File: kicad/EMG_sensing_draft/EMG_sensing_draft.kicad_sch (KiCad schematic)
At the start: 99 parts, among them J1 USB_A_0480370001, J2 EMG_SIGNAL, J3 DEBUG, U1 MCP6N11-002E/SN, U2 W25Q128JV, U3 ISL90462WIH627Z-TKCT-ND, U4 RP2040, U5 RN4871-I/RM140, U6 MCP1702T-3302E_CB, U8 MCP6024T-E/ST, Y1 12MHz

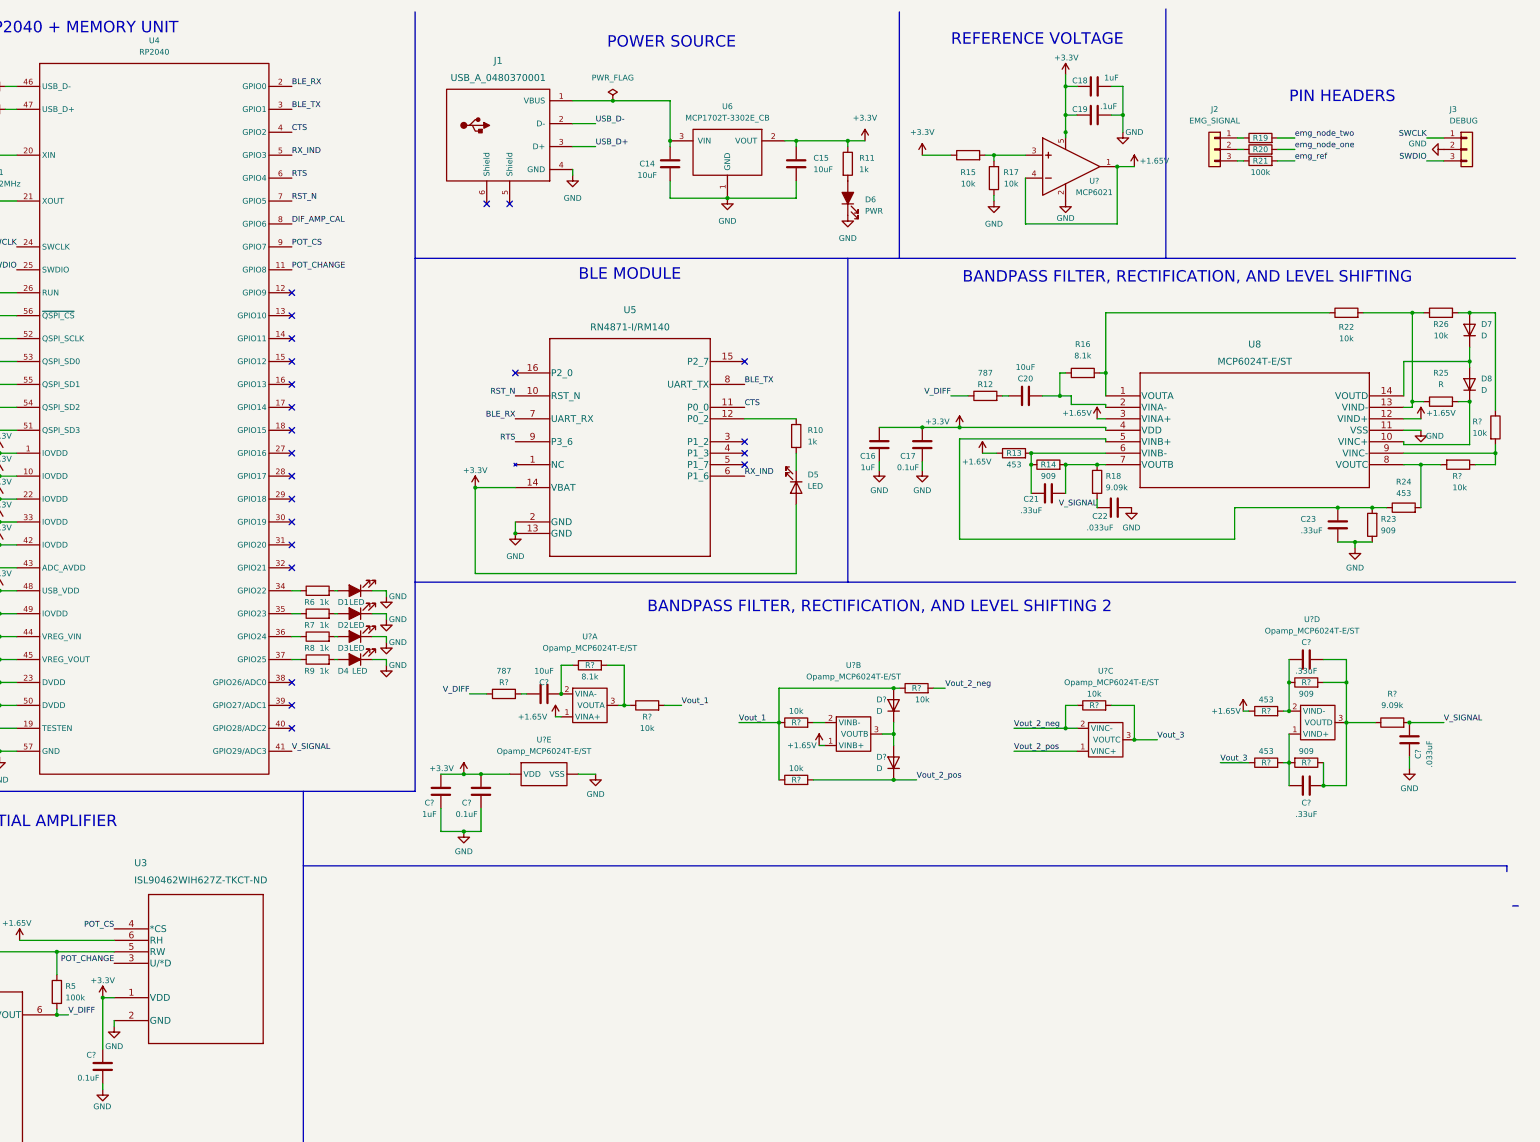
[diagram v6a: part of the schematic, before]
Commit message: fixed ble pin connection
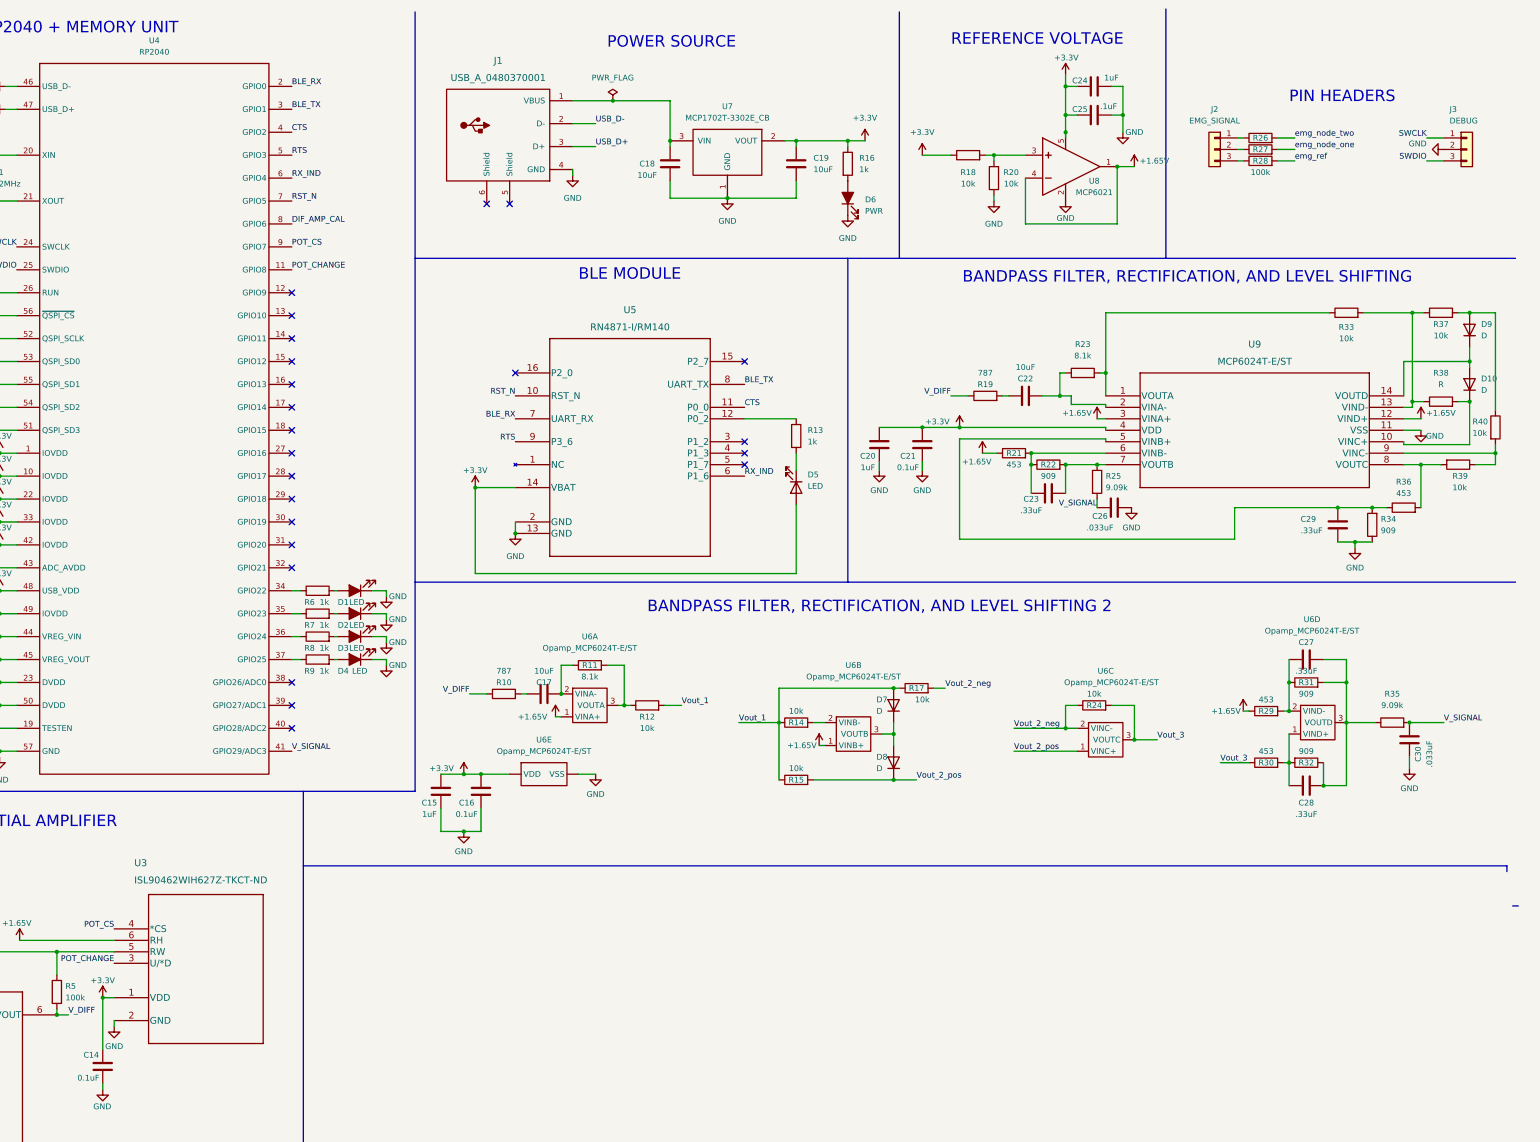
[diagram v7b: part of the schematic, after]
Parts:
- gave numbers to parts that had none: 25
- renumbered C14 to C18, C15 to C19, C16 to C20, C17 to C21, C20 to C22, C21 to C23, C18 to C24, C19 to C25, C22 to C26, C23 to C29, D8 to D10, D7 to D9, R10 to R13, R11 to R16, R15 to R18, R12 to R19, R17 to R20, R13 to R21, R14 to R22, R16 to R23, R18 to R25, R19 to R26, R20 to R27, R21 to R28, R22 to R33, R23 to R34, R24 to R36, R26 to R37, R25 to R38, U6 to U7, U8 to U9
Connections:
- net RTS: now also U4.5 (GPIO3); no longer U4.6 (GPIO4)
- net RX_IND: now also U4.6 (GPIO4); no longer U4.5 (GPIO3)

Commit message: Add Brad suggestions
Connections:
- net +1.65V: now also U3.5 (RW); no longer U3.6 (RH)
- net RTS: now also U4.6 (GPIO4); no longer U4.5 (GPIO3)
- net RX_IND: now also U4.5 (GPIO3); no longer U4.6 (GPIO4)
- net at R5.2, U1.1 (VFG): now also U3.6 (RH); no longer U3.5 (RW)
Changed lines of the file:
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@@
   (junction (at 22.86 105.41) (diameter 0) (color 0 0 0 0)
   )
-  (junction (at 85.09 220.98) (diameter 0) (color 0 0 0 0)
-  )
   (junction (at 398.145 90.17) (diameter 0) (color 0 0 0 0)
   )
+  (junction (at 85.09 220.98) (diameter 0) (color 0 0 0 0)
+  )
   (junction (at 403.86 110.49) (diameter 0) (color 0 0 0 0)
   )
@@
     (stroke (width 0) (type default) (color 0 0 0 0))
   )
-  (wire (pts (xy 85.09 220.98) (xy 97.79 220.98))
-    (stroke (width 0) (type default) (color 0 0 0 0))
-  )
   (wire (pts (xy 290.83 44.45) (xy 292.735 44.45))
     (stroke (width 0) (type default) (color 0 0 0 0))
@@
     (stroke (width 0) (type default) (color 0 0 0 0))
   )
-  (wire (pts (xy 76.835 218.44) (xy 97.79 218.44))
-    (stroke (width 0) (type default) (color 0 0 0 0))
-  )
   (wire (pts (xy 307.34 92.71) (xy 308.61 92.71))
     (stroke (width 0) (type default) (color 0 0 0 0))
@@
     (stroke (width 0) (type default) (color 0 0 0 0))
   )
+  (wire (pts (xy 85.09 220.98) (xy 85.09 217.17))
+    (stroke (width 0) (type default) (color 0 0 0 0))
+  )
   (wire (pts (xy 359.41 45.72) (xy 355.6 45.72))
     (stroke (width 0) (type default) (color 0 0 0 0))
@@
     (stroke (width 0) (type default) (color 0 0 0 0))
   )
+  (wire (pts (xy 97.79 224.79) (xy 97.79 223.52))
+    (stroke (width 0) (type default) (color 0 0 0 0))
+  )
   (wire (pts (xy 71.12 130.81) (xy 72.39 130.81))
     (stroke (width 0) (type default) (color 0 0 0 0))
@@
     (stroke (width 0) (type default) (color 0 0 0 0))
   )
+  (wire (pts (xy 97.79 217.17) (xy 97.79 218.44))
+    (stroke (width 0) (type default) (color 0 0 0 0))
+  )
   (wire (pts (xy 72.39 110.49) (xy 76.2 110.49))
     (stroke (width 0) (type default) (color 0 0 0 0))
@@
     (stroke (width 0) (type default) (color 0 0 0 0))
   )
+  (wire (pts (xy 97.79 212.09) (xy 97.79 215.9))
+    (stroke (width 0) (type default) (color 0 0 0 0))
+  )
   (wire (pts (xy 59.69 115.57) (xy 63.5 115.57))
     (stroke (width 0) (type default) (color 0 0 0 0))
@@
     (stroke (width 0) (type default) (color 0 0 0 0))
   )
+  (wire (pts (xy 85.09 217.17) (xy 97.79 217.17))
+    (stroke (width 0) (type default) (color 0 0 0 0))
+  )
   (wire (pts (xy 72.39 171.45) (xy 76.2 171.45))
     (stroke (width 0) (type default) (color 0 0 0 0))
@@
     (stroke (width 0) (type default) (color 0 0 0 0))
   )
+  (wire (pts (xy 95.25 220.98) (xy 97.79 220.98))
+    (stroke (width 0) (type default) (color 0 0 0 0))
+  )
   (wire (pts (xy 309.88 99.695) (xy 317.5 99.695))
     (stroke (width 0) (type default) (color 0 0 0 0))
@@
     (effects (font (size 1.27 1.27)) (justify left bottom))
   )
-  (label "POT_CS" (at 97.79 215.9 180)
+  (label "POT_CS" (at 97.79 212.09 180)
     (effects (font (size 1.27 1.27)) (justify right bottom))
   )
@@
     (effects (font (size 1.27 1.27)) (justify right bottom))
   )
-  (label "RTS" (at 137.16 44.45 0)
+  (label "RTS" (at 137.16 49.53 0)
     (effects (font (size 1.27 1.27)) (justify left bottom))
   )
@@
     (effects (font (size 1.27 1.27)) (justify left bottom))
   )
-  (label "POT_CHANGE" (at 97.79 223.52 180)
+  (label "POT_CHANGE" (at 97.79 224.79 180)
     (effects (font (size 1.27 1.27)) (justify right bottom))
   )
@@
     (effects (font (size 1.27 1.27)) (justify right bottom))
   )
-  (label "RX_IND" (at 137.16 49.53 0)
+  (label "RX_IND" (at 137.16 44.45 0)
     (effects (font (size 1.27 1.27)) (justify left bottom))
   )
@@
     (pin "1")
   )
-  (symbol (lib_name "+1.65V_3") (lib_id "Eclectronics:+1.65V") (at 76.835 214.63 0) (unit 1)
-    (in_bom yes) (on_board yes)
-    (property "Reference" "#PWR22" (id 0) (at 82.169 219.837 0)
-      (effects (font (size 1.27 1.27)) hide)
-    )
-    (property "Value" "+1.65V" (id 1) (at 76.2 214.63 0))
-    (property "Footprint" "" (id 2) (at 76.835 214.63 0)
-      (effects (font (size 1.27 1.27)) hide)
-    )
-    (property "Datasheet" "" (id 3) (at 76.835 214.63 0)
-      (effects (font (size 1.27 1.27)) hide)
-    )
-    (pin "1")
-  )
   (symbol (lib_id "Device:C") (at 170.18 185.42 180) (unit 1)
     (in_bom yes) (on_board yes)
@@
     (pin "")
   )
+  (symbol (lib_name "+1.65V_3") (lib_id "Eclectronics:+1.65V") (at 95.25 217.17 0) (unit 1)
+    (in_bom yes) (on_board yes)
+    (property "Reference" "#PWR22" (id 0) (at 100.584 222.377 0)
+      (effects (font (size 1.27 1.27)) hide)
+    )
+    (property "Value" "+1.65V" (id 1) (at 90.17 219.71 0))
+    (property "Footprint" "" (id 2) (at 95.25 217.17 0)
+      (effects (font (size 1.27 1.27)) hide)
+    )
+    (property "Datasheet" "" (id 3) (at 95.25 217.17 0)
+      (effects (font (size 1.27 1.27)) hide)
+    )
+    (pin "1")
+  )
   (symbol (lib_name "+1.65V_3") (lib_id "Eclectronics:+1.65V") (at 254 171.45 0) (unit 1)
     (in_bom yes) (on_board yes)
@@
       (reference "#PWR021") (unit 1) (value "GND") (footprint "")
     )
-    (path "/535b0d29-90b9-4661-a80a-72a180fbec78"
+    (path "/ac997eb5-6f0f-4346-89ed-a610d0d20512"
       (reference "#PWR22") (unit 1) (value "+1.65V") (footprint "")
     )
